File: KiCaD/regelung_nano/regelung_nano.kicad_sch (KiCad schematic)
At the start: 12 parts

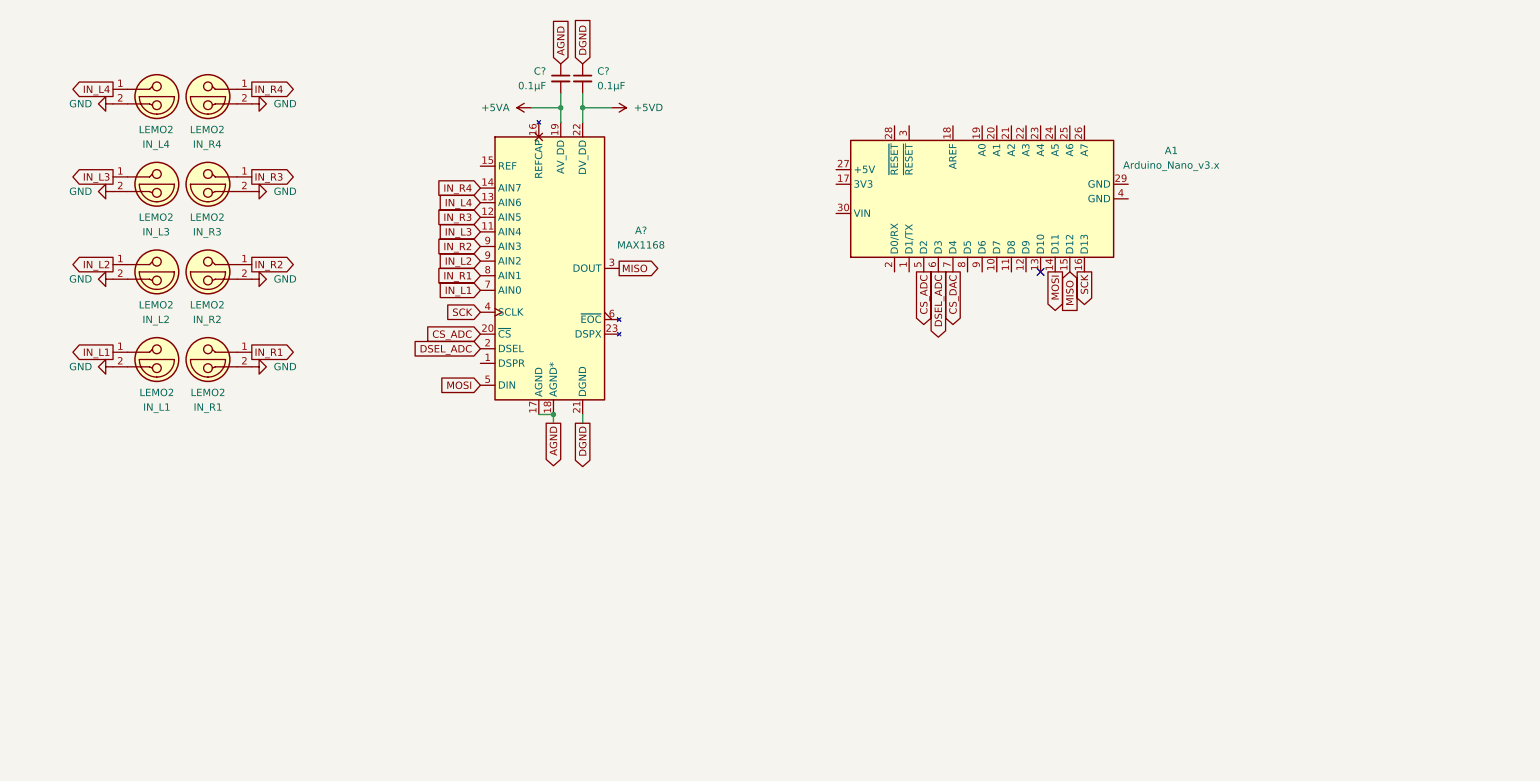
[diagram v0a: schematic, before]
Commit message: ENH:updated schematik for ICs to use
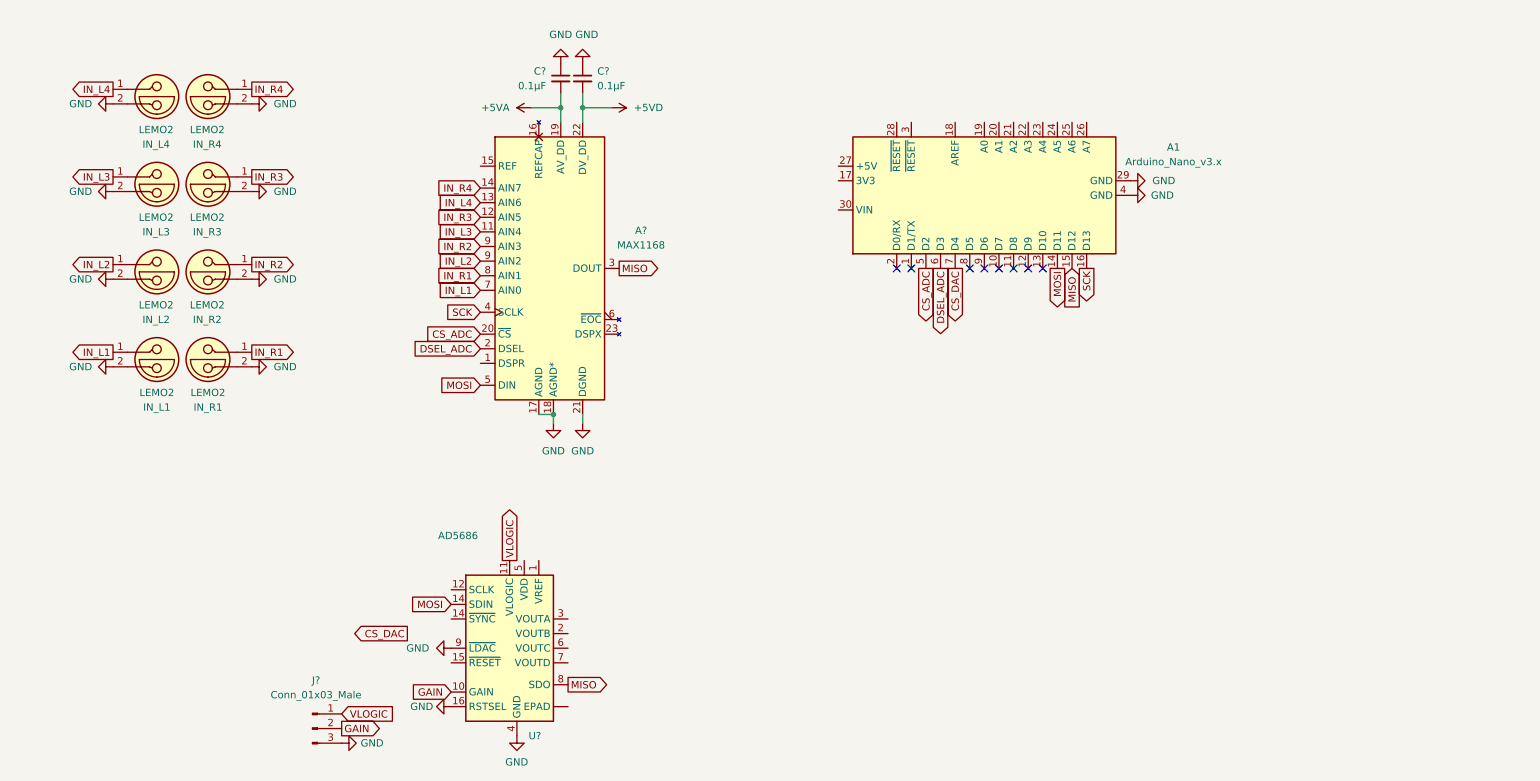
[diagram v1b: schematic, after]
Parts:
- added J?: Conn_01x03_Male, symbol Connector:Conn_01x03_Male
- added U?: AD5686, OwnFootprints:AD5686, symbol Analog_DAC:AD5686
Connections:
- net AGND is gone; now on net GND: A?.17 (AGND), A?.18 (AGND*), C?.1
- net DGND is gone; now on net GND: A?.21 (DGND), C?.1
- net GND: now also A1.29 (GND), A1.4 (GND), J?.3 (Pin_3), U?.16 (RSTSEL), U?.4 (GND), U?.9 (~{LDAC})
- net MISO: now also U?.8 (SDO)
- net MOSI: now also U?.14 (~{SYNC})
- new net GAIN: J?.2 (Pin_2), U?.10 (GAIN)
- new net VLOGIC: J?.1 (Pin_1), U?.11 (VLOGIC)
- no-connect marks 1 -> 8
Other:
- moved on the sheet: A1

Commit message: FIX: adc communication via SPI now working via given SPIComm library
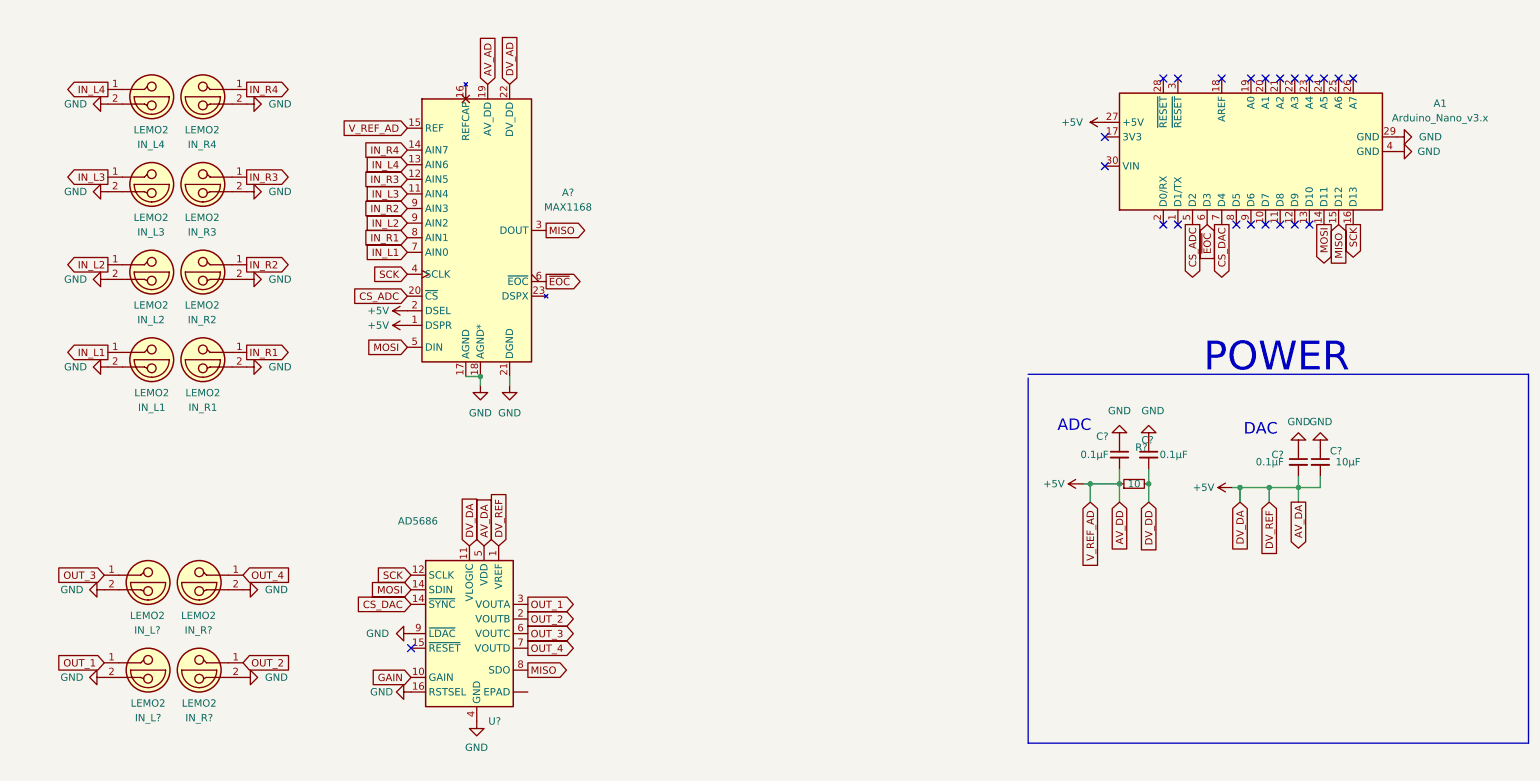
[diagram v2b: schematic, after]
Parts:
- removed J?: Conn_01x03_Male, symbol Connector:Conn_01x03_Male
- added C?: 10µF, Capacitor_SMD:CP_Elec_3x5.3, symbol Device:C_Small
- added C?: 0.1µF, Capacitor_SMD:CP_Elec_3x5.3, symbol Device:C_Small
- added IN_L? (x2), IN_R? (x2): LEMO2, symbol Connector:LEMO2
- added R?: 10, Resistor_SMD:R_0201_0603Metric, symbol Device:R_Small
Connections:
- net VLOGIC is gone; now on net +5V: U?.11 (VLOGIC)
- net CS_DAC: now also U?.14 (~{SYNC})
- net GND: now also C?.1, C?.1, IN_L?.2, IN_L?.2, IN_R?.2, IN_R?.2
- net SCK: now also U?.12 (SCLK)
- net +5V: now reaches A1.27 (+5V)
- net +5V: now also A?.1 (DSPR), A?.15 (REF), A?.2 (DSEL), C?.2, U?.1 (VREF), U?.5 (VDD), C?.2, C?.2, R?.1
- net OUT_2: now reaches U?.2 (VOUTB)
- net OUT_2: now also IN_R?.1
- net OUT_1: now reaches U?.3 (VOUTA)
- net OUT_1: now also IN_L?.1
- net OUT_3: now reaches U?.6 (VOUTC)
- net OUT_3: now also IN_L?.1
- net OUT_4: now reaches U?.7 (VOUTD)
- net OUT_4: now also IN_R?.1
- net ~{EOC}: now reaches A?.6 (~{EOC})
- net ~{EOC}: now also A1.6 (D3)
- net +5VA renamed AV_AD
- net AV_AD: no longer C?.2
- net +5VD renamed DV_AD
- net DV_AD: no longer C?.2
- removed net DSEL_ADC: A1.6 (D3), A?.2 (DSEL)
- new net DV_DD: C?.2, R?.2
- no-connect marks 8 -> 22
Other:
- note added: "ADC"
- note added: "DAC"
- note added: "POWER"
- moved on the sheet: A1, C?, IN_L1, IN_L2, IN_L3, IN_L4, IN_R1, IN_R2, IN_R3, IN_R4, U?

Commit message: ADD: change SPI library to work with ADC in use
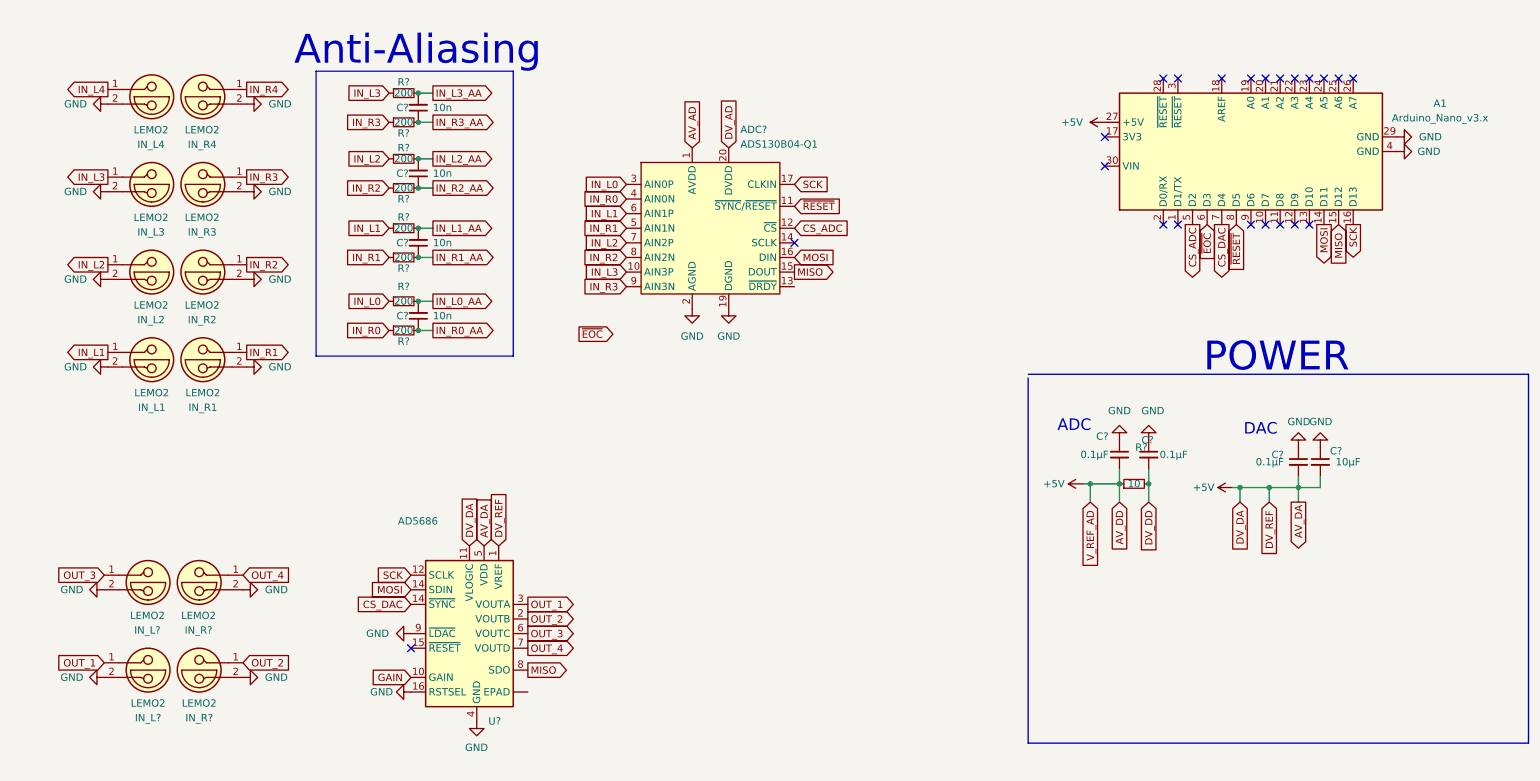
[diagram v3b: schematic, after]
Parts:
- removed A?: MAX1168, symbol Analog_ADC:MAX1168
- added ADC?: ADS130B04-Q1, Package_SO:TSSOP-20_4.4x6.5mm_P0.65mm, symbol Analog_ADC:ADS130B04-Q1
- added C? (x4): 10n, Capacitor_SMD:CP_Elec_3x5.3, symbol Device:C_Small
- added R? (x8): 200, Resistor_SMD:R_0201_0603Metric, symbol Device:R_Small
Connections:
- net AV_AD: now also ADC?.1 (AVDD)
- net CS_ADC: now also ADC?.12 (~{CS})
- net DV_AD: now also ADC?.20 (DVDD)
- net GND: now also ADC?.19 (DGND), ADC?.2 (AGND)
- net IN_L1: now also ADC?.6 (AIN1P), R?.1
- net IN_L2: now also ADC?.7 (AIN2P), R?.1
- net IN_L3: now also ADC?.10 (AIN3P), R?.1
- net IN_R1: now also ADC?.5 (AIN1N), R?.1
- net IN_R2: now also ADC?.8 (AIN2N), R?.1
- net IN_R3: now also ADC?.9 (AIN3N), R?.1
- net MISO: now also ADC?.15 (DOUT)
- net MOSI: now also ADC?.16 (DIN)
- net SCK: now also ADC?.17 (CLKIN)
- net ~{RESET}: now reaches A1.8 (D5)
- net ~{RESET}: now also ADC?.11 (~{SYNC}/~{RESET})
- new net IN_L0: ADC?.3 (AIN0P), R?.1
- new net IN_L0_AA: C?.2, R?.2
- new net IN_L1_AA: C?.2, R?.2
- new net IN_L2_AA: C?.2, R?.2
- new net IN_L3_AA: C?.2, R?.2
- new net IN_R0: ADC?.4 (AIN0N), R?.1
- new net IN_R0_AA: C?.1, R?.2
- new net IN_R1_AA: C?.1, R?.2
- new net IN_R2_AA: C?.1, R?.2
- new net IN_R3_AA: C?.1, R?.2
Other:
- note added: "Anti-Aliasing"

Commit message: ENH: update schematic
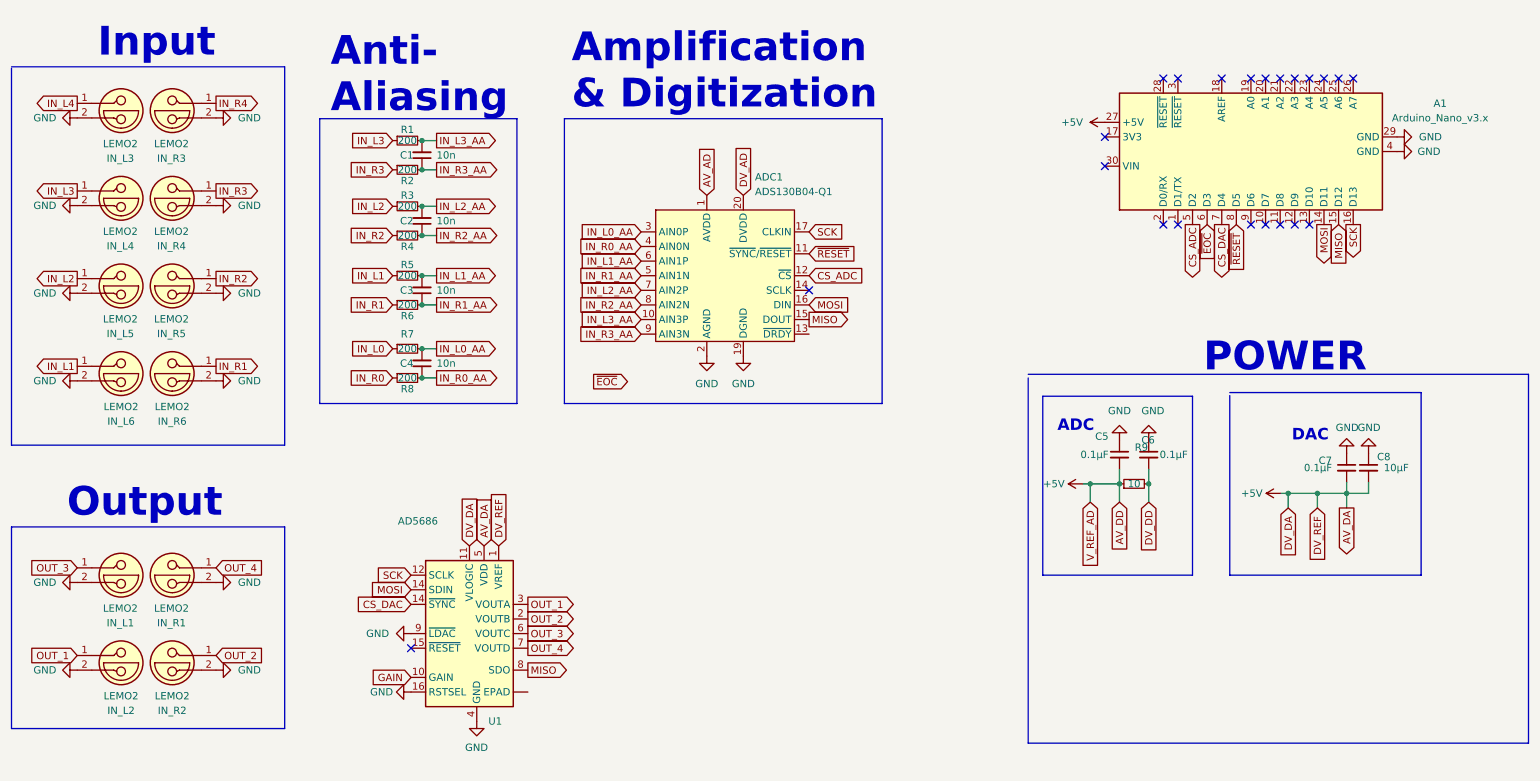
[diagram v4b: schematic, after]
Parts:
- gave numbers to parts that had none: 23
- renumbered IN_L4 to IN_L3, IN_L3 to IN_L4, IN_L2 to IN_L5, IN_L1 to IN_L6, IN_R4 to IN_R3, IN_R3 to IN_R4, IN_R2 to IN_R5, IN_R1 to IN_R6
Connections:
- net IN_L0: no longer ADC1.3 (AIN0P)
- net IN_L0_AA: now also ADC1.3 (AIN0P)
- net IN_L1: no longer ADC1.6 (AIN1P)
- net IN_L1_AA: now also ADC1.6 (AIN1P)
- net IN_L2: no longer ADC1.7 (AIN2P)
- net IN_L2_AA: now also ADC1.7 (AIN2P)
- net IN_L3: no longer ADC1.10 (AIN3P)
- net IN_L3_AA: now also ADC1.10 (AIN3P)
- net IN_R0: no longer ADC1.4 (AIN0N)
- net IN_R0_AA: now also ADC1.4 (AIN0N)
- net IN_R1: no longer ADC1.5 (AIN1N)
- net IN_R1_AA: now also ADC1.5 (AIN1N)
- net IN_R2: no longer ADC1.8 (AIN2N)
- net IN_R2_AA: now also ADC1.8 (AIN2N)
- net IN_R3: no longer ADC1.9 (AIN3N)
- net IN_R3_AA: now also ADC1.9 (AIN3N)
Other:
- note added: "Amplification & Digitization"
- note added: "Anti- Aliasing"
- note added: "Input"
- note added: "Output"
- note removed: "Anti-Aliasing"
- moved on the sheet: ADC1, C1, C2, C3, C4, C7, C8, IN_L1, IN_L2, IN_L3, IN_L4, IN_L5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
